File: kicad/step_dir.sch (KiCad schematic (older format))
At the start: 17 parts, among them J1001 tblock2x6, U1001 am26ls32a

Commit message: change in 5v interface scenario.. remove bridges
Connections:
- net labels added: 5VI, GNDI
- net labels removed: 5VH, GNDH
- wire segments 91 -> 111
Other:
- moved on the sheet: JP1001

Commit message: added sloted holes everyware
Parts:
- removed JP1001: jumper, servo:SolderJumper-2_P1.3mm_Open_RoundedPad1.0x1.5mm, symbol servo:jumper
- removed JP1002: jumper, Jumper:SolderJumper-3_P1.3mm_Open_RoundedPad1.0x1.5mm, symbol servo:Jumper_3_Bridged12
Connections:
- net labels removed: Earth, STEP_DiR_5VH
- wire segments 111 -> 106
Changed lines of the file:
@@
 	8900 4150 9000 4150
 Wire Wire Line
-	8850 2050 8950 2050
-Wire Wire Line
-	8950 2050 8950 2000
+	8650 2150 8650 2100
 Wire Wire Line
 	7400 4050 8400 4050
@@
 	0    1    1    0
 $EndComp
-$Comp
-L servo:Jumper_3_Bridged12 JP?
-U 1 1 5E302920
-P 8650 4350
-AR Path="/5E1BAEAA/5E302920" Ref="JP?"  Part="1"
-AR Path="/5E21534F/5E302920" Ref="JP?"  Part="1"
-AR Path="/5DE3DF56/5E302920" Ref="JP1002"  Part="1"
-F 0 "JP1002" H 8650 4519 39  0000 C CNN
-F 1 "jumper" H 8650 4444 39  0000 C CNN
-F 2 "Jumper:SolderJumper-3_P1.3mm_Open_RoundedPad1.0x1.5mm" H 8450 4150 50  0001 C CNN
-F 3 "~" H 8550 4250 50  0001 C CNN
-	1    8650 4350
-	1    0    0    1
-$EndComp
-Wire Wire Line
-	8300 4250 8650 4250
-Wire Wire Line
-	8650 4250 9000 4250
-Connection ~ 8650 4250
 Text Label 8150 4050 0    20   ~ 0
 DIR1_A_N_H
@@
 Wire Wire Line
 	7400 4700 8700 4700
-$Comp
-L servo:Earth #PWR?
-U 1 1 5E302929
-P 8300 4450
-AR Path="/5E21534F/5E302929" Ref="#PWR?"  Part="1"
-AR Path="/5DE3DF56/5E302929" Ref="#PWR0222"  Part="1"
-F 0 "#PWR0222" H 8300 4200 20  0001 C CNN
-F 1 "Earth" H 8300 4300 20  0000 C CNN
-F 2 "" H 8300 4450 50  0001 C CNN
-F 3 "~" H 8300 4450 50  0001 C CNN
-	1    8300 4450
-	1    0    0    -1
-$EndComp
-Wire Wire Line
-	8300 4450 8300 4350
-Wire Wire Line
-	8300 4350 8450 4350
-$Comp
-L servo:jumper JP?
-U 1 1 5E2CFB11
-P 8750 2050
-AR Path="/5DD76B18/5E2CFB11" Ref="JP?"  Part="1"
-AR Path="/5DE3DF56/5E2CFB11" Ref="JP1001"  Part="1"
-F 0 "JP1001" H 8750 2211 39  0000 C CNN
-F 1 "jumper" H 8750 2136 39  0000 C CNN
-F 2 "servo:SolderJumper-2_P1.3mm_Open_RoundedPad1.0x1.5mm" H 8650 2030 50  0001 C CNN
-F 3 "~" H 8750 2130 50  0001 C CNN
-	1    8750 2050
-	1    0    0    -1
-$EndComp
-Wire Wire Line
-	8650 2050 8650 2150
 Connection ~ 8650 2150
-Text Label 8400 2150 0    20   ~ 0
-STEP_DiR_5VH
 Text Label 8800 4250 0    20   ~ 0
 STEP_DiR_GND
@@
 L servo:5VI #PWR?
 U 1 1 5E388B36
-P 8950 2000
+P 8650 2100
 AR Path="/5DD76B18/5E388B36" Ref="#PWR?"  Part="1"
-AR Path="/5DE3DF56/5E388B36" Ref="#PWR?"  Part="1"
-F 0 "#PWR?" H 8950 1800 20  0001 C CNN
-F 1 "5VI" H 8950 2157 28  0000 C CNN
-F 2 "" H 8950 2000 50  0001 C CNN
-F 3 "" H 8950 2000 50  0001 C CNN
-	1    8950 2000
+AR Path="/5DE3DF56/5E388B36" Ref="#PWR0141"  Part="1"
+F 0 "#PWR0141" H 8650 1900 20  0001 C CNN
+F 1 "5VI" H 8650 2257 28  0000 C CNN
+F 2 "" H 8650 2100 50  0001 C CNN
+F 3 "" H 8650 2100 50  0001 C CNN
+	1    8650 2100
 	1    0    0    -1
 $EndComp
@@
 Connection ~ 9800 2150
 $Comp
-L servo:GNDI #PWR?
+L servo:GNDI #PWR0142
 U 1 1 5E39F025
-P 9000 4350
-F 0 "#PWR?" H 9000 4100 30  0001 C CNN
-F 1 "GNDI" H 9000 4201 20  0000 C CNN
-F 2 "" H 9000 4350 50  0001 C CNN
-F 3 "" H 9000 4350 50  0001 C CNN
-	1    9000 4350
+P 8600 7100
+F 0 "#PWR0142" H 8600 6850 30  0001 C CNN
+F 1 "GNDI" H 8600 6951 20  0000 C CNN
+F 2 "" H 8600 7100 50  0001 C CNN
+F 3 "" H 8600 7100 50  0001 C CNN
+	1    8600 7100
 	1    0    0    -1
 $EndComp
 Wire Wire Line
 	10100 5950 10100 7100
-Wire Wire Line
-	8850 4350 9000 4350
 Wire Wire Line
 	7800 5450 7500 5450
@@
 	7500 5450 6750 5450
 Wire Wire Line
-	7500 7100 10100 7100
+	7500 7100 8600 7100
 Wire Wire Line
 	7500 5800 7500 7100
@@
 Wire Wire Line
 	8650 3550 9050 3550
+Wire Wire Line
+	8300 4250 9000 4250
+Connection ~ 8600 7100
+Wire Wire Line
+	8600 7100 10100 7100
 $EndSCHEMATC

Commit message: serigrafia...
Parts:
- R1001, R1002, R1003, R1004, R1005, R1006, R1007, R1008, R1009, R1010, R1011, R1012: footprint Resistor_SMD:R_0603_1608Metric -> servo:R_0603_1608Metric
- U1001: footprint Package_SO:SOIC-16W_5.3x10.2mm_P1.27mm -> servo:SOIC-16W_5.3x10.2mm_P1.27mm
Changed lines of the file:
@@
 F 0 "R1001" H 7209 2922 20  0000 L CNN
 F 1 "10k" H 7209 2879 20  0000 L CNN
-F 2 "Resistor_SMD:R_0603_1608Metric" H 7150 2900 50  0001 C CNN
+F 2 "servo:R_0603_1608Metric" H 7150 2900 50  0001 C CNN
 F 3 "~" H 7150 2900 50  0001 C CNN
 	1    7150 2900
@@
 F 0 "R1002" H 7209 3122 20  0000 L CNN
 F 1 "1k" H 7209 3079 20  0000 L CNN
-F 2 "Resistor_SMD:R_0603_1608Metric" H 7150 3100 50  0001 C CNN
+F 2 "servo:R_0603_1608Metric" H 7150 3100 50  0001 C CNN
 F 3 "~" H 7150 3100 50  0001 C CNN
 	1    7150 3100
@@
 F 0 "R1003" H 7209 3322 20  0000 L CNN
 F 1 "10k" H 7209 3279 20  0000 L CNN
-F 2 "Resistor_SMD:R_0603_1608Metric" H 7150 3300 50  0001 C CNN
+F 2 "servo:R_0603_1608Metric" H 7150 3300 50  0001 C CNN
 F 3 "~" H 7150 3300 50  0001 C CNN
 	1    7150 3300
@@
 F 0 "R1004" H 7559 2922 20  0000 L CNN
 F 1 "10k" H 7559 2879 20  0000 L CNN
-F 2 "Resistor_SMD:R_0603_1608Metric" H 7500 2900 50  0001 C CNN
+F 2 "servo:R_0603_1608Metric" H 7500 2900 50  0001 C CNN
 F 3 "~" H 7500 2900 50  0001 C CNN
 	1    7500 2900
@@
 F 0 "R1005" H 7559 3122 20  0000 L CNN
 F 1 "1k" H 7559 3079 20  0000 L CNN
-F 2 "Resistor_SMD:R_0603_1608Metric" H 7500 3100 50  0001 C CNN
+F 2 "servo:R_0603_1608Metric" H 7500 3100 50  0001 C CNN
 F 3 "~" H 7500 3100 50  0001 C CNN
 	1    7500 3100
@@
 F 0 "R1006" H 7559 3322 20  0000 L CNN
 F 1 "10k" H 7559 3279 20  0000 L CNN
-F 2 "Resistor_SMD:R_0603_1608Metric" H 7500 3300 50  0001 C CNN
+F 2 "servo:R_0603_1608Metric" H 7500 3300 50  0001 C CNN
 F 3 "~" H 7500 3300 50  0001 C CNN
 	1    7500 3300
@@
 F 0 "R1010" H 10209 2922 20  0000 L CNN
 F 1 "10k" H 10209 2879 20  0000 L CNN
-F 2 "Resistor_SMD:R_0603_1608Metric" H 10150 2900 50  0001 C CNN
+F 2 "servo:R_0603_1608Metric" H 10150 2900 50  0001 C CNN
 F 3 "~" H 10150 2900 50  0001 C CNN
 	1    10150 2900
@@
 F 0 "R1011" H 10209 3122 20  0000 L CNN
 F 1 "1k" H 10209 3079 20  0000 L CNN
-F 2 "Resistor_SMD:R_0603_1608Metric" H 10150 3100 50  0001 C CNN
+F 2 "servo:R_0603_1608Metric" H 10150 3100 50  0001 C CNN
 F 3 "~" H 10150 3100 50  0001 C CNN
 	1    10150 3100
@@
 F 0 "R1012" H 10209 3322 20  0000 L CNN
 F 1 "10k" H 10209 3279 20  0000 L CNN
-F 2 "Resistor_SMD:R_0603_1608Metric" H 10150 3300 50  0001 C CNN
+F 2 "servo:R_0603_1608Metric" H 10150 3300 50  0001 C CNN
 F 3 "~" H 10150 3300 50  0001 C CNN
 	1    10150 3300
@@
 F 0 "R1007" H 9859 2922 20  0000 L CNN
 F 1 "10k" H 9859 2879 20  0000 L CNN
-F 2 "Resistor_SMD:R_0603_1608Metric" H 9800 2900 50  0001 C CNN
+F 2 "servo:R_0603_1608Metric" H 9800 2900 50  0001 C CNN
 F 3 "~" H 9800 2900 50  0001 C CNN
 	1    9800 2900
@@
 F 0 "R1008" H 9859 3122 20  0000 L CNN
 F 1 "1k" H 9859 3079 20  0000 L CNN
-F 2 "Resistor_SMD:R_0603_1608Metric" H 9800 3100 50  0001 C CNN
+F 2 "servo:R_0603_1608Metric" H 9800 3100 50  0001 C CNN
 F 3 "~" H 9800 3100 50  0001 C CNN
 	1    9800 3100
@@
 F 0 "R1009" H 9859 3322 20  0000 L CNN
 F 1 "10k" H 9859 3279 20  0000 L CNN
-F 2 "Resistor_SMD:R_0603_1608Metric" H 9800 3300 50  0001 C CNN
+F 2 "servo:R_0603_1608Metric" H 9800 3300 50  0001 C CNN
 F 3 "~" H 9800 3300 50  0001 C CNN
 	1    9800 3300
@@
 F 0 "U1001" H 8800 7000 39  0000 C CNN
 F 1 "am26ls32a" H 8750 6900 39  0000 C CNN
-F 2 "Package_SO:SOIC-16W_5.3x10.2mm_P1.27mm" H 9950 5000 50  0001 C CNN
+F 2 "servo:SOIC-16W_5.3x10.2mm_P1.27mm" H 9950 5000 50  0001 C CNN
 F 3 "../doc/datasheets/am26ls32a.pdf" H 8950 5550 50  0001 C CNN
 	1    8950 5950

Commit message: bom bom bom...
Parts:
- C1001: value 100nF -> 0.1uF; PartNumber (none) -> CC0603KPX7R7BB104; digikey (none) -> 311-1335-1-ND
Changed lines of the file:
@@
 AR Path="/5DE3DF56/5F04EFB4" Ref="C1001"  Part="1"
 F 0 "C1001" V 7528 5710 20  0000 L CNN
-F 1 "100nF" V 7571 5710 20  0000 L CNN
+F 1 "0.1uF" V 7571 5710 20  0000 L CNN
 F 2 "servo:C_0603_1608Metric" H 7500 5500 60  0001 C CNN
 F 3 "" H 7500 5600 60  0000 C CNN
+F 4 "CC0603KPX7R7BB104" H 0   0   50  0001 C CNN "PartNumber"
+F 5 "311-1335-1-ND" H 0   0   50  0001 C CNN "digikey"
 	1    7500 5600
 	0    1    1    0

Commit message: more bom...
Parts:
- C1001: Description (none) -> CAP CER 0.1UF 16V X7R 0603
- J1001: value tblock2x6 -> tblock 2x6 3.81; Description (none) -> 12 Position Terminal Block Header, Male Pins, Shrouded (4 S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; PartNumber (none) -> 1843114; digikey (none) -> 277-6009-ND; price@10 (none) -> 7.50500
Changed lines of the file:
@@
 AR Path="/5F8D42C2/6322E1B9" Ref="J?"  Part="1"
 F 0 "J1001" H 8650 4243 39  0000 C CNN
-F 1 "tblock2x6" H 8650 4168 39  0000 C CNN
+F 1 "tblock 2x6 3.81" H 8650 4168 39  0000 C CNN
 F 2 "servo:tblock02x6_3.81" H 8550 4050 50  0001 C CNN
-F 3 "../doc/datasheets/tblock2rows.pdf" H 8650 4150 50  0001 C CNN
+F 3 "" H 8650 4150 50  0001 C CNN
+F 4 "12 Position Terminal Block Header, Male Pins, Shrouded (4 Side) 0.150\" (3.81mm) 90°, Right Angle Through Hole " H 0   0   50  0001 C CNN "Description"
+F 5 "1843114 " H 0   0   50  0001 C CNN "PartNumber"
+F 6 "277-6009-ND " H 0   0   50  0001 C CNN "digikey"
+F 7 "7.50500" H 0   0   50  0001 C CNN "price@10"
 	1    8600 3850
 	1    0    0    -1
@@
 F 4 "CC0603KPX7R7BB104" H 0   0   50  0001 C CNN "PartNumber"
 F 5 "311-1335-1-ND" H 0   0   50  0001 C CNN "digikey"
+F 6 "CAP CER 0.1UF 16V X7R 0603 " H 0   0   50  0001 C CNN "Description"
 	1    7500 5600
 	0    1    1    0

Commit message: stackup
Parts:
- C1001: price@10 (none) -> 0.05800
- U1001: Description (none) -> 0/4 Receiver RS422, RS423 16-SOIC; PartNumber (none) -> AM26LS32ACDR; digikey (none) -> 296-1011-1-ND; price@10 (none) -> 0.57800
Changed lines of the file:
@@
 F 2 "servo:SOIC-16W_5.3x10.2mm_P1.27mm" H 9950 5000 50  0001 C CNN
 F 3 "../doc/datasheets/am26ls32a.pdf" H 8950 5550 50  0001 C CNN
+F 4 "0/4 Receiver RS422, RS423 16-SOIC " H 0   0   50  0001 C CNN "Description"
+F 5 "AM26LS32ACDR " H 0   0   50  0001 C CNN "PartNumber"
+F 6 "296-1011-1-ND" H 0   0   50  0001 C CNN "digikey"
+F 7 "0.57800" H 0   0   50  0001 C CNN "price@10"
 	1    8950 5950
 	0    -1   1    0
@@
 F 5 "311-1335-1-ND" H 0   0   50  0001 C CNN "digikey"
 F 6 "CAP CER 0.1UF 16V X7R 0603 " H 0   0   50  0001 C CNN "Description"
+F 7 "0.05800" H 0   0   50  0001 C CNN "price@10"
 	1    7500 5600
 	0    1    1    0

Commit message: bom copleted
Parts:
- R1001, R1003, R1004, R1006, R1007, R1009, R1010, R1012: Description (none) -> 10 kOhms ±5% 0.1W, 1/10W Chip Resistor 0603 (1608 Metric) M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; PartNumber (none) -> RC0603JR-0710KL; digikey (none) -> 311-10KGRCT-ND; price@10 (none) -> 0.01900
- R1002, R1005, R1008, R1011: Description (none) -> 1 kOhms ±5% 0.1W, 1/10W Chip Resistor 0603 (1608 Metric) Mo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; PartNumber (none) -> RC0603JR-071KL; digikey (none) -> 311-1.0KGRCT-ND; price@10 (none) -> 0.01900
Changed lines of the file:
@@
 F 2 "servo:R_0603_1608Metric" H 7150 2900 50  0001 C CNN
 F 3 "~" H 7150 2900 50  0001 C CNN
+F 4 "10 kOhms ±5% 0.1W, 1/10W Chip Resistor 0603 (1608 Metric) Moisture Resistant Thick Film " H 0   0   50  0001 C CNN "Description"
+F 5 "RC0603JR-0710KL" H 0   0   50  0001 C CNN "PartNumber"
+F 6 "311-10KGRCT-ND" H 0   0   50  0001 C CNN "digikey"
+F 7 "0.01900" H 0   0   50  0001 C CNN "price@10"
 	1    7150 2900
 	1    0    0    -1
@@
 F 2 "servo:R_0603_1608Metric" H 7150 3100 50  0001 C CNN
 F 3 "~" H 7150 3100 50  0001 C CNN
+F 4 "1 kOhms ±5% 0.1W, 1/10W Chip Resistor 0603 (1608 Metric) Moisture Resistant Thick Film " H 0   0   50  0001 C CNN "Description"
+F 5 "RC0603JR-071KL" H 0   0   50  0001 C CNN "PartNumber"
+F 6 "311-1.0KGRCT-ND" H 0   0   50  0001 C CNN "digikey"
+F 7 "0.01900" H 0   0   50  0001 C CNN "price@10"
 	1    7150 3100
 	1    0    0    -1
@@
 F 2 "servo:R_0603_1608Metric" H 7150 3300 50  0001 C CNN
 F 3 "~" H 7150 3300 50  0001 C CNN
+F 4 "10 kOhms ±5% 0.1W, 1/10W Chip Resistor 0603 (1608 Metric) Moisture Resistant Thick Film " H 0   0   50  0001 C CNN "Description"
+F 5 "RC0603JR-0710KL" H 0   0   50  0001 C CNN "PartNumber"
+F 6 "311-10KGRCT-ND" H 0   0   50  0001 C CNN "digikey"
+F 7 "0.01900" H 0   0   50  0001 C CNN "price@10"
 	1    7150 3300
 	1    0    0    -1
@@
 F 2 "servo:R_0603_1608Metric" H 7500 2900 50  0001 C CNN
 F 3 "~" H 7500 2900 50  0001 C CNN
+F 4 "10 kOhms ±5% 0.1W, 1/10W Chip Resistor 0603 (1608 Metric) Moisture Resistant Thick Film " H 0   0   50  0001 C CNN "Description"
+F 5 "RC0603JR-0710KL" H 0   0   50  0001 C CNN "PartNumber"
+F 6 "311-10KGRCT-ND" H 0   0   50  0001 C CNN "digikey"
+F 7 "0.01900" H 0   0   50  0001 C CNN "price@10"
 	1    7500 2900
 	1    0    0    -1
@@
 F 2 "servo:R_0603_1608Metric" H 7500 3100 50  0001 C CNN
 F 3 "~" H 7500 3100 50  0001 C CNN
+F 4 "1 kOhms ±5% 0.1W, 1/10W Chip Resistor 0603 (1608 Metric) Moisture Resistant Thick Film " H 0   0   50  0001 C CNN "Description"
+F 5 "RC0603JR-071KL" H 0   0   50  0001 C CNN "PartNumber"
+F 6 "311-1.0KGRCT-ND" H 0   0   50  0001 C CNN "digikey"
+F 7 "0.01900" H 0   0   50  0001 C CNN "price@10"
 	1    7500 3100
 	1    0    0    -1
@@
 F 2 "servo:R_0603_1608Metric" H 7500 3300 50  0001 C CNN
 F 3 "~" H 7500 3300 50  0001 C CNN
+F 4 "10 kOhms ±5% 0.1W, 1/10W Chip Resistor 0603 (1608 Metric) Moisture Resistant Thick Film " H 0   0   50  0001 C CNN "Description"
+F 5 "RC0603JR-0710KL" H 0   0   50  0001 C CNN "PartNumber"
+F 6 "311-10KGRCT-ND" H 0   0   50  0001 C CNN "digikey"
+F 7 "0.01900" H 0   0   50  0001 C CNN "price@10"
 	1    7500 3300
 	1    0    0    -1
@@
 F 2 "servo:R_0603_1608Metric" H 10150 2900 50  0001 C CNN
 F 3 "~" H 10150 2900 50  0001 C CNN
+F 4 "10 kOhms ±5% 0.1W, 1/10W Chip Resistor 0603 (1608 Metric) Moisture Resistant Thick Film " H 0   0   50  0001 C CNN "Description"
+F 5 "RC0603JR-0710KL" H 0   0   50  0001 C CNN "PartNumber"
+F 6 "311-10KGRCT-ND" H 0   0   50  0001 C CNN "digikey"
+F 7 "0.01900" H 0   0   50  0001 C CNN "price@10"
 	1    10150 2900
 	-1   0    0    -1
@@
 F 2 "servo:R_0603_1608Metric" H 10150 3100 50  0001 C CNN
 F 3 "~" H 10150 3100 50  0001 C CNN
+F 4 "1 kOhms ±5% 0.1W, 1/10W Chip Resistor 0603 (1608 Metric) Moisture Resistant Thick Film " H 0   0   50  0001 C CNN "Description"
+F 5 "RC0603JR-071KL" H 0   0   50  0001 C CNN "PartNumber"
+F 6 "311-1.0KGRCT-ND" H 0   0   50  0001 C CNN "digikey"
+F 7 "0.01900" H 0   0   50  0001 C CNN "price@10"
 	1    10150 3100
 	-1   0    0    -1
@@
 F 2 "servo:R_0603_1608Metric" H 10150 3300 50  0001 C CNN
 F 3 "~" H 10150 3300 50  0001 C CNN
+F 4 "10 kOhms ±5% 0.1W, 1/10W Chip Resistor 0603 (1608 Metric) Moisture Resistant Thick Film " H 0   0   50  0001 C CNN "Description"
+F 5 "RC0603JR-0710KL" H 0   0   50  0001 C CNN "PartNumber"
+F 6 "311-10KGRCT-ND" H 0   0   50  0001 C CNN "digikey"
+F 7 "0.01900" H 0   0   50  0001 C CNN "price@10"
 	1    10150 3300
 	-1   0    0    -1
@@
 F 2 "servo:R_0603_1608Metric" H 9800 2900 50  0001 C CNN
 F 3 "~" H 9800 2900 50  0001 C CNN
+F 4 "10 kOhms ±5% 0.1W, 1/10W Chip Resistor 0603 (1608 Metric) Moisture Resistant Thick Film " H 0   0   50  0001 C CNN "Description"
+F 5 "RC0603JR-0710KL" H 0   0   50  0001 C CNN "PartNumber"
+F 6 "311-10KGRCT-ND" H 0   0   50  0001 C CNN "digikey"
+F 7 "0.01900" H 0   0   50  0001 C CNN "price@10"
 	1    9800 2900
 	-1   0    0    -1
@@
 F 2 "servo:R_0603_1608Metric" H 9800 3100 50  0001 C CNN
 F 3 "~" H 9800 3100 50  0001 C CNN
+F 4 "1 kOhms ±5% 0.1W, 1/10W Chip Resistor 0603 (1608 Metric) Moisture Resistant Thick Film " H 0   0   50  0001 C CNN "Description"
+F 5 "RC0603JR-071KL" H 0   0   50  0001 C CNN "PartNumber"
+F 6 "311-1.0KGRCT-ND" H 0   0   50  0001 C CNN "digikey"
+F 7 "0.01900" H 0   0   50  0001 C CNN "price@10"
 	1    9800 3100
 	-1   0    0    -1
@@
 F 2 "servo:R_0603_1608Metric" H 9800 3300 50  0001 C CNN
 F 3 "~" H 9800 3300 50  0001 C CNN
+F 4 "10 kOhms ±5% 0.1W, 1/10W Chip Resistor 0603 (1608 Metric) Moisture Resistant Thick Film " H 0   0   50  0001 C CNN "Description"
+F 5 "RC0603JR-0710KL" H 0   0   50  0001 C CNN "PartNumber"
+F 6 "311-10KGRCT-ND" H 0   0   50  0001 C CNN "digikey"
+F 7 "0.01900" H 0   0   50  0001 C CNN "price@10"
 	1    9800 3300
 	-1   0    0    -1

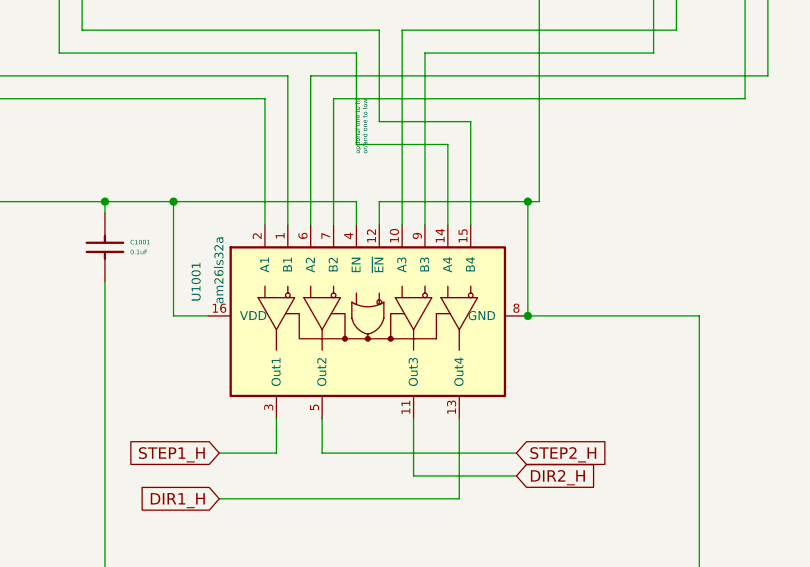
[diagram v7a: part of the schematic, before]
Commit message: changes in footprints
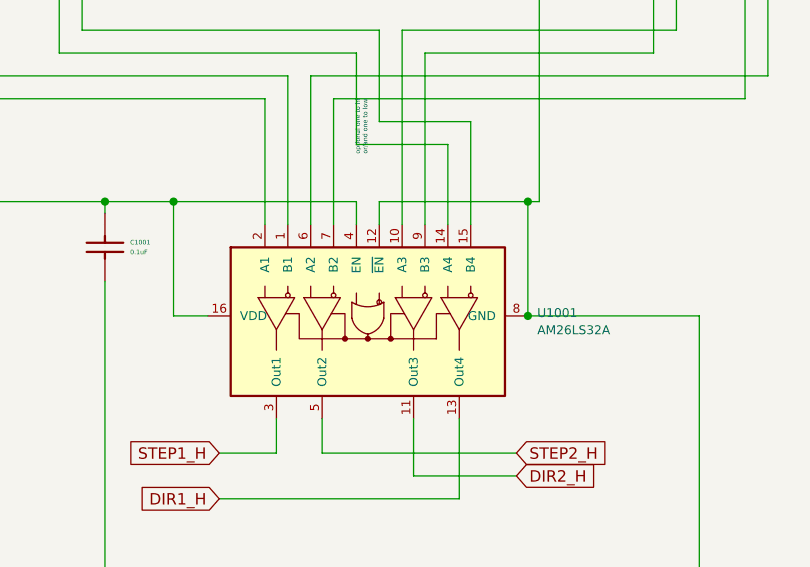
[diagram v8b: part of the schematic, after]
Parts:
- U1001: value am26ls32a -> AM26LS32A; PartNumber AM26LS32ACDR -> AM26LS32ACDR
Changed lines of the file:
@@
 AR Path="/5E092156/6322E22C" Ref="U1001"  Part="1"
 AR Path="/5DE3DF56/6322E22C" Ref="U1001"  Part="1"
-F 0 "U1001" H 8800 7000 39  0000 C CNN
-F 1 "am26ls32a" H 8750 6900 39  0000 C CNN
+F 0 "U1001" V 8937 5509 39  0000 R CNN
+F 1 "AM26LS32A" V 9012 5509 39  0000 R CNN
 F 2 "servo:SOIC-16W_5.3x10.2mm_P1.27mm" H 9950 5000 50  0001 C CNN
 F 3 "../doc/datasheets/am26ls32a.pdf" H 8950 5550 50  0001 C CNN
 F 4 "0/4 Receiver RS422, RS423 16-SOIC " H 0   0   50  0001 C CNN "Description"
-F 5 "AM26LS32ACDR " H 0   0   50  0001 C CNN "PartNumber"
+F 5 "AM26LS32ACDR" H 0   0   50  0001 C CNN "PartNumber"
 F 6 "296-1011-1-ND" H 0   0   50  0001 C CNN "digikey"
 F 7 "0.57800" H 0   0   50  0001 C CNN "price@10"
